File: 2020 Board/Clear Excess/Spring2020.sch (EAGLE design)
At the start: 37 parts

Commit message: Started building up new board & cleanup
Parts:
- removed C13, C14: (no value), resistor:C-US025-050X050
- removed C3, C6: (no value), resistor:C-US025-025X050
- removed R6, R9: (no value), resistor:R-US_0613/15
- removed RE2: (no value), con-lstb:MA04-2
- removed VREGULATOR: 7818DT, linear:7818DT
- added SV1: (no value), con-lstb:MA03-2
- BIKEMOTOR: device con-lstb:MA04-1 -> con-lstb:MA03-1
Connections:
- removed net 22: R1.1, U$1.22
- removed net 2CIN1: C6.1, LR2.CIN1, R9.2, RE2.4
- removed net 2CIN2: C3.1, LR2.CIN2, R6.1, RE2.3
- removed net 2COUT: LR2.COUT, U$1.A6
- removed net VIN: U$1.VIN
- new net LED1: R1.1
- new net N$4: BIKEMOTOR.1
- new net N$5: LR2.EN
- net 2AIN1: now also SV1.6; no longer RE2.8
- net 2AIN2: now also SV1.5; no longer RE2.7
- net 2AOUT: no longer U$1.2
- net 2BIN1: now also SV1.4; no longer RE2.6
- net 2BIN2: now also SV1.3; no longer RE2.5
- net 2BOUT: no longer U$1.13
- net 3.3V: no longer R6.2, R9.1, U$1.3V3
- net 5V: now also SV1.2; no longer RE2.2, U$1.5V
- net BAT+: no longer C13.1, VREGULATOR.VI
- net BGND: no longer C13.2, C14.2, VREGULATOR.GND
- net FRONT-DIGIOUT: no longer BIKEMOTOR.2
- net FRONT-PWMOUT/SERVO1: no longer BIKEMOTOR.1
- net GND: now also SV1.1; no longer C3.2, C6.2, RC.7, RE2.1, U$1.5V_ICSP, U$1.GND_1, U$1.GND_2
- net IMU-CS: no longer U$1.A11
- net LR-EN: no longer LR2.EN
- net N$3: now also BIKEMOTOR.2; no longer BIKEMOTOR.3
- net REAR-TIMER: now also BIKEMOTOR.3; no longer BIKEMOTOR.4
- net REG5V: no longer C14.1, VREGULATOR.VO
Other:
- moved on the sheet: IMU, LED1, R1, RC

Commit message: Some more cleanup
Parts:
- removed C1, C2, C4, C5: (no value), resistor:C-US025-025X050
- removed C22: (no value), resistor:C-US025-050X050
- removed LR2: ST26C32ABDR, BikeTeamLR:ST26C32ABDR
- removed R4, R5, R7, R8: (no value), resistor:R-US_0613/15
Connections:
- removed net 2AIN1: C4.1, LR2.AIN1, R7.2, SV1.6
- removed net 2AIN2: C1.1, LR2.AIN2, R4.1, SV1.5
- removed net 2AOUT: LR2.AOUT
- removed net 2BIN1: C5.1, LR2.BIN1, R8.2, SV1.4
- removed net 2BIN2: C2.1, LR2.BIN2, R5.1, SV1.3
- removed net 2BOUT: LR2.BOUT
- removed net N$2: C22.1
- removed net N$5: LR2.EN
- net 3.3V: no longer C22.2, LR2.VCC, R4.2, R5.2, R7.1, R8.1
- net 5V: no longer SV1.2
- net GND: no longer C1.2, C2.2, C4.2, C5.2, LR2.DIN1, LR2.DIN2, LR2.GND, SV1.1

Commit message: Final Cleaning of Bike
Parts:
- removed BIKEMOTOR, SERVO1, SERVO2: (no value), con-lstb:MA03-1
- removed C20: (no value), resistor:C-US025-050X050
- removed OP-AMP: OPAMP, Spring2016opamp:OPAMP
- removed SV1: (no value), con-lstb:MA03-2
- removed U$1: DUE(NORMAL), DUElib130425:DUE(NORMAL)
- added REAR-MOTOR: (no value), con-lstb:MA04-1
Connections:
- removed net 29: U$1.29
- removed net BAT+: SERVO1.2, SERVO2.2
- removed net BRAKE: RC.5, U$1.28
- removed net HORN: RC.1, U$1.32
- removed net LR-EN: U$1.26
- removed net N$3: BIKEMOTOR.2, OP-AMP.-IN, OP-AMP.OUT
- removed net N$4: BIKEMOTOR.1
- removed net PANIC: RC.2, U$1.27
- removed net REV: RC.3, U$1.33
- new net CH3: RC.3
- new net CH4: RC.4
- new net CH5: RC.5
- new net CH6: RC.6
- new net REVERSE: REAR-MOTOR.3
- net BGND: now also REAR-MOTOR.1; no longer C20.2, OP-AMP.V-, SERVO1.3, SERVO2.3
- net CH1: now also RC.1; no longer RC.6, U$1.51
- net CH2: now also RC.2; no longer RC.4, U$1.25
- net FRONT-DIGI: no longer U$1.46
- net FRONT-PWM: no longer U$1.9
- net FRONT-PWMOUT/SERVO1: no longer SERVO1.1
- net GND: now also RC.7
- net MISO: no longer U$1.MISO_ICSP
- net MOSI: no longer U$1.MOSI_ICSP
- net REAR-PWM: no longer U$1.8
- net REAR-PWMOUT: now also REAR-MOTOR.2; no longer OP-AMP.+IN
- net REAR-PWMR/SERVO2: no longer SERVO2.1
- net REAR-TIMER: now also REAR-MOTOR.4; no longer BIKEMOTOR.3
- net REAR-TIMER-IN: no longer U$1.11
- net REG5V: no longer C20.1, OP-AMP.V+
- net SCK: no longer U$1.SCK_ICSP
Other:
- note removed: "Op-Amp"
- moved on the sheet: BIKE-PWR-1, BIKE-PWR-2, C15, C16, C18, C19, GND-JUMPER, IMU, LED1, R1, RC

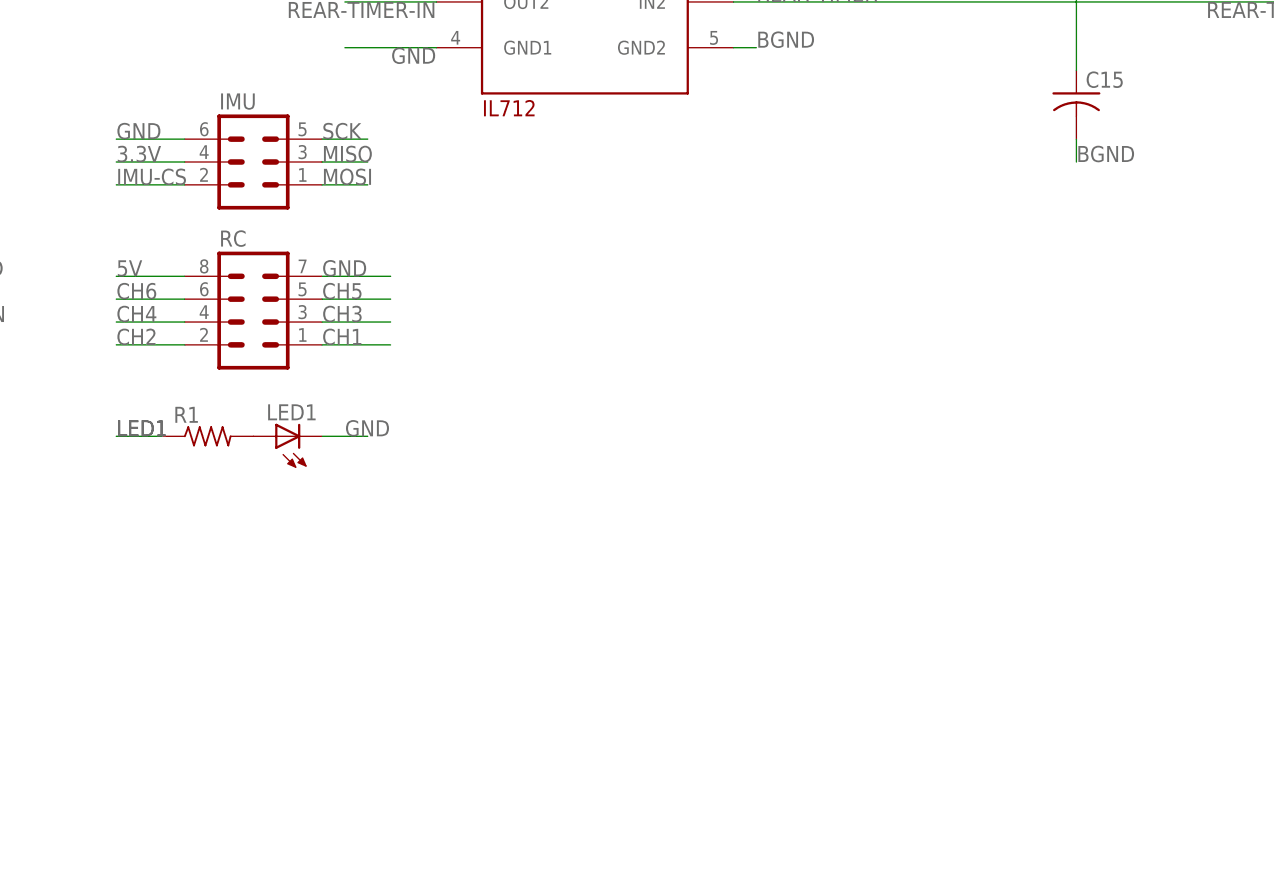
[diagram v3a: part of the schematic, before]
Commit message: MCR
Added the front motor controller, once clarification comes in on the isolator, can deal with the isolator connection as well
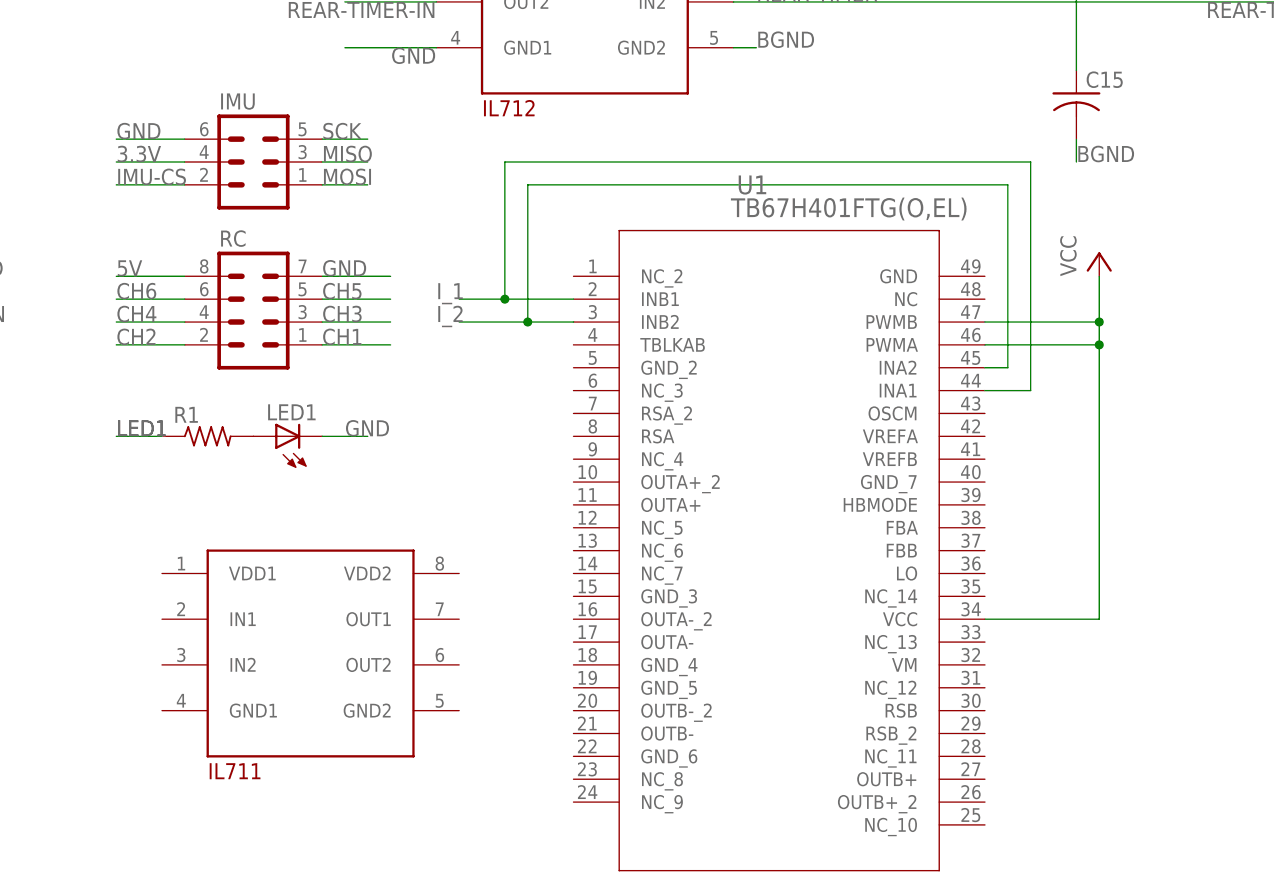
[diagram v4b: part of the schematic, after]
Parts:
- added U$1: IL-711, Spring2016Optoisolator:IL-711
- added U1: TB67H401FTG(O,EL), mclr:TB67H401FTG(O,EL)
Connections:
- new net I_1: U1.INA1, U1.INB1
- new net I_2: U1.INA2, U1.INB2
- new net VCC: U1.PWMA, U1.PWMB, U1.VCC
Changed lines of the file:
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@@
 <layer number="54" name="bGND_GNDA" color="1" fill="9" visible="no" active="no"/>
 <layer number="56" name="wert" color="7" fill="1" visible="no" active="no"/>
+<layer number="88" name="SimResults" color="9" fill="1" visible="yes" active="yes"/>
+<layer number="89" name="SimProbes" color="9" fill="1" visible="yes" active="yes"/>
 <layer number="90" name="Modules" color="5" fill="1" visible="yes" active="yes"/>
 <layer number="91" name="Nets" color="2" fill="1" visible="yes" active="yes"/>
@@
 <part name="U$7" library="Spring2016Optoisolator" deviceset="IL-712" device=""/>
 <part name="GND-JUMPER" library="jumper" deviceset="JP1E" device=""/>
+<part name="U1" library="mclr" deviceset="TB67H401FTG(O,EL)" device=""/>
+<part name="P+1" library="supply1" library_urn="urn:adsk.eagle:library:371" deviceset="VCC" device=""/>
+<part name="U$1" library="Spring2016Optoisolator" deviceset="IL-711" device=""/>
 </parts>
 <sheets>
@@
 <attribute name="VALUE" x="91.44" y="69.215" size="1.778" layer="96" rot="R180"/>
 </instance>
+<instance part="U1" gate="A" x="167.64" y="88.9" smashed="yes">
+<attribute name="NAME" x="188.3156" y="98.0186" size="2.0828" layer="95" ratio="6" rot="SR0"/>
+<attribute name="VALUE" x="187.6806" y="95.4786" size="2.0828" layer="96" ratio="6" rot="SR0"/>
+</instance>
+<instance part="P+1" gate="VCC" x="228.6" y="91.44" smashed="yes">
+<attribute name="VALUE" x="226.06" y="88.9" size="1.778" layer="96" rot="R90"/>
+</instance>
+<instance part="U$1" gate="G$1" x="137.16" y="38.1" smashed="yes"/>
 </instances>
 <busses>
@@
 </segment>
 </net>
+<net name="I_1" class="0">
+<segment>
+<pinref part="U1" gate="A" pin="INB1"/>
+<wire x1="170.18" y1="86.36" x2="162.56" y2="86.36" width="0.1524" layer="91"/>
+<pinref part="U1" gate="A" pin="INA1"/>
+<wire x1="215.9" y1="76.2" x2="220.98" y2="76.2" width="0.1524" layer="91"/>
+<wire x1="220.98" y1="76.2" x2="220.98" y2="101.6" width="0.1524" layer="91"/>
+<wire x1="220.98" y1="101.6" x2="162.56" y2="101.6" width="0.1524" layer="91"/>
+<wire x1="162.56" y1="101.6" x2="162.56" y2="86.36" width="0.1524" layer="91"/>
+<wire x1="162.56" y1="86.36" x2="157.48" y2="86.36" width="0.1524" layer="91"/>
+<junction x="162.56" y="86.36"/>
+<label x="154.94" y="86.36" size="1.778" layer="95"/>
+</segment>
+</net>
+<net name="I_2" class="0">
+<segment>
+<pinref part="U1" gate="A" pin="INA2"/>
+<wire x1="215.9" y1="78.74" x2="218.44" y2="78.74" width="0.1524" layer="91"/>
+<wire x1="218.44" y1="78.74" x2="218.44" y2="99.06" width="0.1524" layer="91"/>
+<wire x1="218.44" y1="99.06" x2="165.1" y2="99.06" width="0.1524" layer="91"/>
+<wire x1="165.1" y1="99.06" x2="165.1" y2="83.82" width="0.1524" layer="91"/>
+<pinref part="U1" gate="A" pin="INB2"/>
+<wire x1="165.1" y1="83.82" x2="170.18" y2="83.82" width="0.1524" layer="91"/>
+<wire x1="165.1" y1="83.82" x2="157.48" y2="83.82" width="0.1524" layer="91"/>
+<junction x="165.1" y="83.82"/>
+<label x="154.94" y="83.82" size="1.778" layer="95"/>
+</segment>
+</net>
+<net name="VCC" class="0">
+<segment>
+<pinref part="U1" gate="A" pin="PWMA"/>
+<wire x1="215.9" y1="81.28" x2="228.6" y2="81.28" width="0.1524" layer="91"/>
+<pinref part="U1" gate="A" pin="PWMB"/>
+<wire x1="215.9" y1="83.82" x2="228.6" y2="83.82" width="0.1524" layer="91"/>
+<wire x1="228.6" y1="81.28" x2="228.6" y2="83.82" width="0.1524" layer="91"/>
+<wire x1="228.6" y1="83.82" x2="228.6" y2="88.9" width="0.1524" layer="91"/>
+<junction x="228.6" y="83.82"/>
+<pinref part="P+1" gate="VCC" pin="VCC"/>
+<pinref part="U1" gate="A" pin="VCC"/>
+<wire x1="215.9" y1="50.8" x2="228.6" y2="50.8" width="0.1524" layer="91"/>
+<wire x1="228.6" y1="50.8" x2="228.6" y2="81.28" width="0.1524" layer="91"/>
+<junction x="228.6" y="81.28"/>
+</segment>
+</net>
